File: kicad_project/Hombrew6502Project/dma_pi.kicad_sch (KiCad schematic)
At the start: 62 parts, among them J201 ICSP Header, J202 PeripheralBusB, J203 EXT INT, J204 I2C, J205 Conn_01x09_Pin, J206 Conn_02x05_Counter_Clockwise, J207 Conn_02x05_Counter_Clockwise, J208 SPI AUX, J209 I2C BUS, J210 UART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

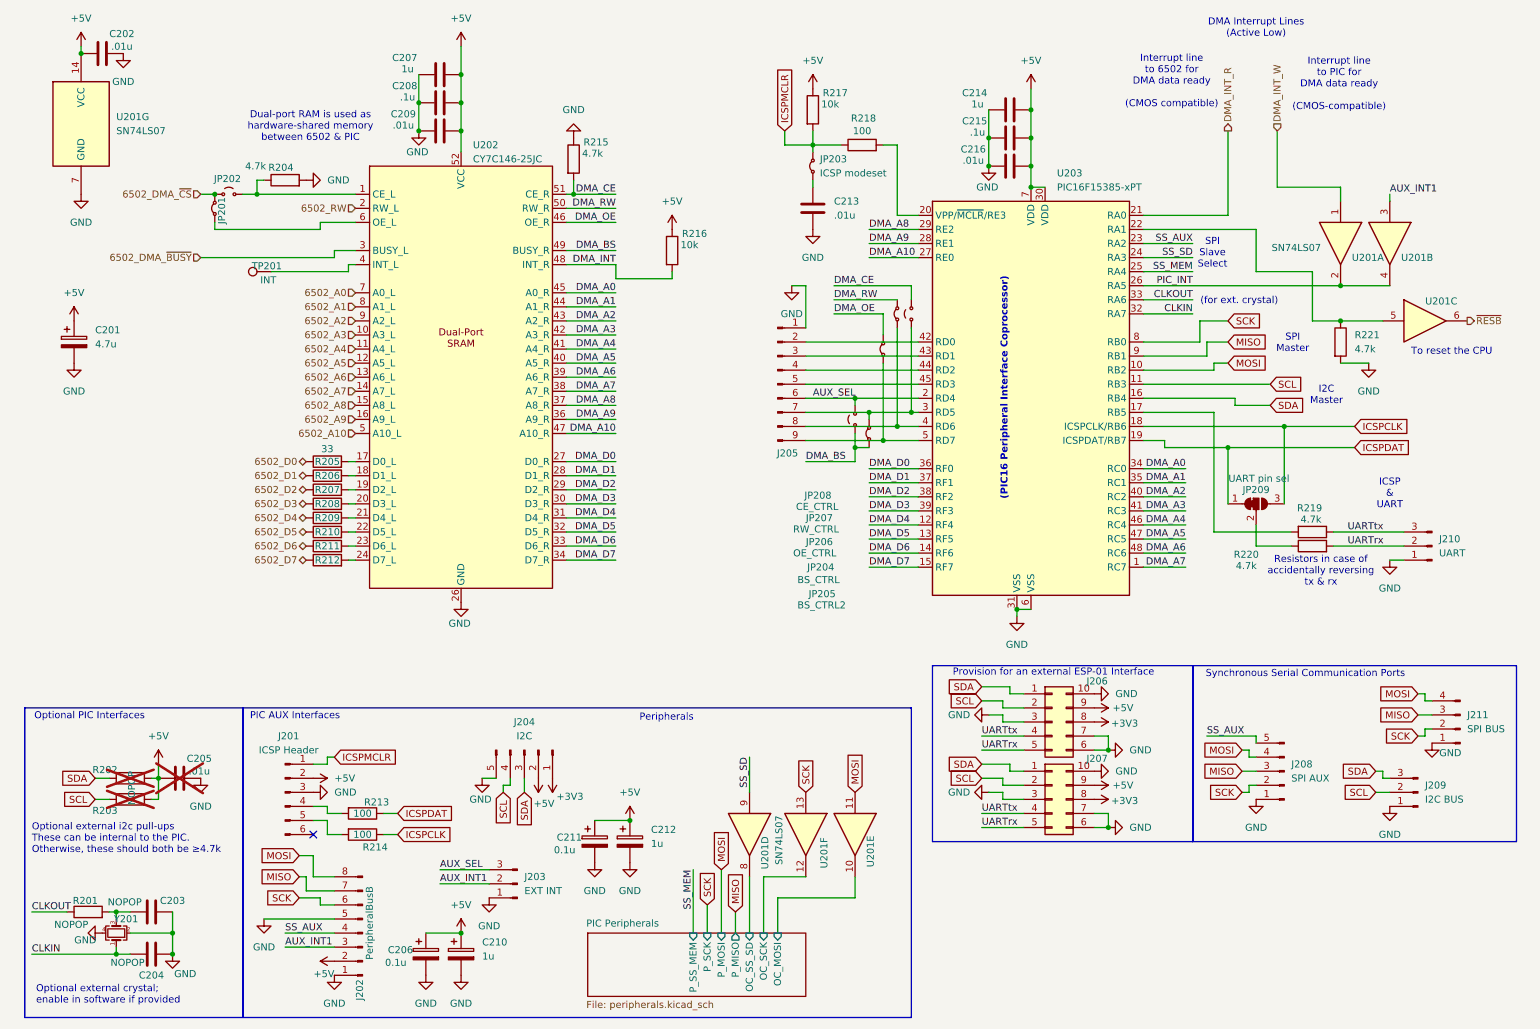
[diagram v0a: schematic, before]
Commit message: Some connector changes
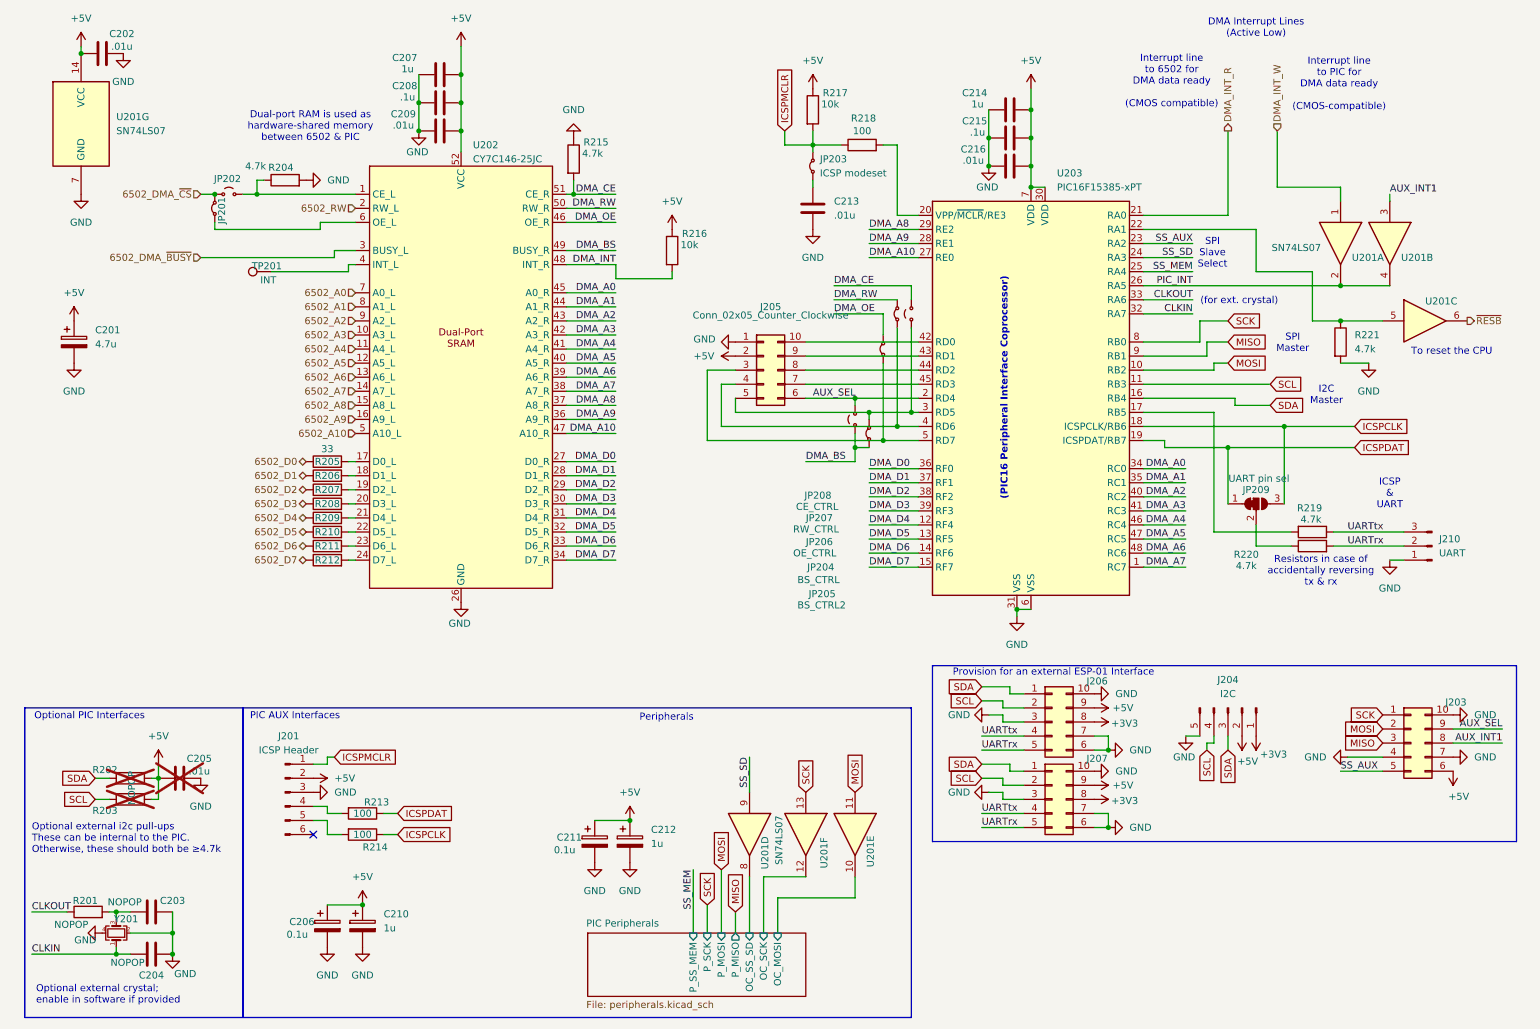
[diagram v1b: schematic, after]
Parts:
- removed J202: PeripheralBusB, symbol Connector:Conn_01x08_Pin
- removed J203: EXT INT, symbol Connector:Conn_01x03_Pin
- removed J205: Conn_01x09_Pin, symbol Connector:Conn_01x09_Pin
- removed J208: SPI AUX, symbol Connector:Conn_01x05_Pin
- removed J209: I2C BUS, symbol Connector:Conn_01x03_Pin
- removed J211: SPI BUS, symbol Connector:Conn_01x04_Pin
- added J203, J205: Conn_02x05_Counter_Clockwise, symbol Connector_Generic:Conn_02x05_Counter_Clockwise
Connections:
- net +5V: now also J203.6 (Pin_6), J205.2 (Pin_2)
- net AUX_INT1: now also J203.8 (Pin_8)
- net AUX_SEL: now also J203.9 (Pin_9), J205.6 (Pin_6)
- net GND: now also J203.10 (Pin_10), J203.4 (Pin_4), J203.7 (Pin_7), J205.1 (Pin_1)
- net MISO: now also J203.3 (Pin_3)
- net MOSI: now also J203.2 (Pin_2)
- net SCK: now also J203.1 (Pin_1)
- net SS_AUX: now also J203.5 (Pin_5)
- net at JP205.2 (B), JP208.1 (A), U203.3 (RD5): now also J205.5 (Pin_5)
- net at JP207.1 (A), U203.4 (RD6): now also J205.4 (Pin_4)
- net at U203.42 (RD0): now also J205.10 (Pin_10)
- net at U203.43 (RD1): now also J205.9 (Pin_9)
- net at U203.44 (RD2): now also J205.8 (Pin_8)
- net at U203.45 (RD3): now also J205.7 (Pin_7)
- net at JP206.1 (A), U203.5 (RD7): now also J205.3 (Pin_3)
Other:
- note removed: "Synchronous Serial Communication Ports"
- moved on the sheet: C206, C210, J204

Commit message: footprint assignments and separate project for RAM board
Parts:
- removed J203, J205, J206, J207: Conn_02x05_Counter_Clockwise, symbol Connector_Generic:Conn_02x05_Counter_Clockwise
- added J202, J203, J205, J206: Conn_02x05_Odd_Even, Connector_PinHeader_2.54mm:PinHeader_2x05_P2.54mm_Vertical_SMD, symbol Connector_Generic:Conn_02x05_Odd_Even
- J201: footprint (none) -> Connector_PinHeader_2.54mm:PinHeader_1x06_P2.54mm_Vertical
- J204: footprint (none) -> Connector_PinHeader_2.54mm:PinHeader_1x05_P2.54mm_Vertical
- J210: footprint (none) -> Connector:FanPinHeader_1x03_P2.54mm_Vertical
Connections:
- net +3V3: now also J203.6 (Pin_6), J205.6 (Pin_6)
- net +5V: now also J202.3 (Pin_3), J203.4 (Pin_4), J205.4 (Pin_4), J206.10 (Pin_10)
- net AUX_INT1: now also J206.6 (Pin_6)
- net AUX_SEL: now also J202.10 (Pin_10), J206.4 (Pin_4)
- net GND: now also J202.1 (Pin_1), J203.10 (Pin_10), J203.2 (Pin_2), J203.5 (Pin_5), J203.8 (Pin_8), J205.10 (Pin_10), J205.2 (Pin_2), J205.5 (Pin_5), J205.8 (Pin_8), J206.2 (Pin_2), J206.7 (Pin_7), J206.8 (Pin_8)
- net MISO: now also J206.5 (Pin_5)
- net MOSI: now also J206.3 (Pin_3)
- net SCK: now also J206.1 (Pin_1)
- net SCL: now also J203.3 (Pin_3), J205.3 (Pin_3)
- net SDA: now also J203.1 (Pin_1), J205.1 (Pin_1)
- net SS_AUX: now also J206.9 (Pin_9)
- net UARTrx: now also J203.9 (Pin_9), J205.9 (Pin_9)
- net UARTtx: now also J203.7 (Pin_7), J205.7 (Pin_7)
- net at JP205.2 (B), JP208.1 (A), U203.3 (RD5): now also J202.9 (Pin_9)
- net at JP207.1 (A), U203.4 (RD6): now also J202.7 (Pin_7)
- net at U203.42 (RD0): now also J202.2 (Pin_2)
- net at U203.43 (RD1): now also J202.4 (Pin_4)
- net at U203.44 (RD2): now also J202.6 (Pin_6)
- net at U203.45 (RD3): now also J202.8 (Pin_8)
- net at JP206.1 (A), U203.5 (RD7): now also J202.5 (Pin_5)

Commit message: Peripheral io layout done; snapshot of current state before redoing much of the rest of the layout.
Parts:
- added C217: .01u, Capacitor_SMD:C_0402_1005Metric, symbol Device:C
- added C218: .1u, Capacitor_SMD:C_0402_1005Metric, symbol Device:C
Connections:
- net +5V: now also C217.1, C218.1
- net GND: now also C217.2, C218.2
